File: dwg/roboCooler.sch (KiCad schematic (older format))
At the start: 37 parts, among them J1 CONN_02X25, J10 CONN_01X12, J11 CONN_01X12, J12 CONN_01X04, J13 CONN_01X04, J14 CONN_01X04, J15 CONN_01X04, J2 CONN_02X25, J3 CONN_01X04, J4 CONN_01X04, J5 CONN_01X02, J6 CONN_01X02, J7 CONN_01X02, J8 CONN_01X02, J9 CONN_01X06, P11 CONN_01X12, P12 CONN_01X04, P13 CONN_01X04, P14 CONN_01X04, P15 CONN_01X04, P3 CONN_01X04, P4 CONN_01X04, P5 CONN_01X02, P6 CONN_01X02, P7 CONN_01X02, P8 CONN_01X02, Q1 NMOS, Q2 NMOS, SW1 SW_PUSH, SW2 SW_PUSH, U1 MPR121, U2 4069, U3 HALL_EFFECT, U4 HALL_EFFECT

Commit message: Added pushbuttons to layout
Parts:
- removed P11: CONN_01X12, symbol CONN_01X12
- removed P12, P14: CONN_01X04, symbol CONN_01X04
- removed SW1, SW2: SW_PUSH, symbol SW_PUSH
- removed U1: MPR121, symbol MPR121
- added R12, R13: 10k, Resistors_SMD:R_0805_HandSoldering, symbol R
- added SW1, SW2: SPST_4PIN, roboCooler:D6C90, symbol SPST_4PIN
- D1, D2: footprint (none) -> Diodes_ThroughHole:Diode_P600_Vertical_AnodeUp
- J1, J2: footprint (none) -> Socket_Strips:Socket_Strip_Straight_2x25
- J10: footprint (none) -> Socket_Strips:Socket_Strip_Straight_1x12
- J11: footprint (none) -> Socket_Strips:Socket_Strip_Angled_1x12
- J3: footprint (none) -> Socket_Strips:Socket_Strip_Angled_1x04
- J5, J7: footprint (none) -> Socket_Strips:Socket_Strip_Angled_1x02
- Q1, Q2: footprint (none) -> Transistors_OldSowjetAera:OldSowjetaera_Transistor_Type-II_BigPads
- R1: footprint (none) -> Resistors_SMD:R_0805_HandSoldering
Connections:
- net labels added: PUSH_DB, PUSH_DN, PUSH_UP
- net labels removed: PUSH_1, PUSH_2
- wire segments 23 -> 29
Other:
- moved on the sheet: J9

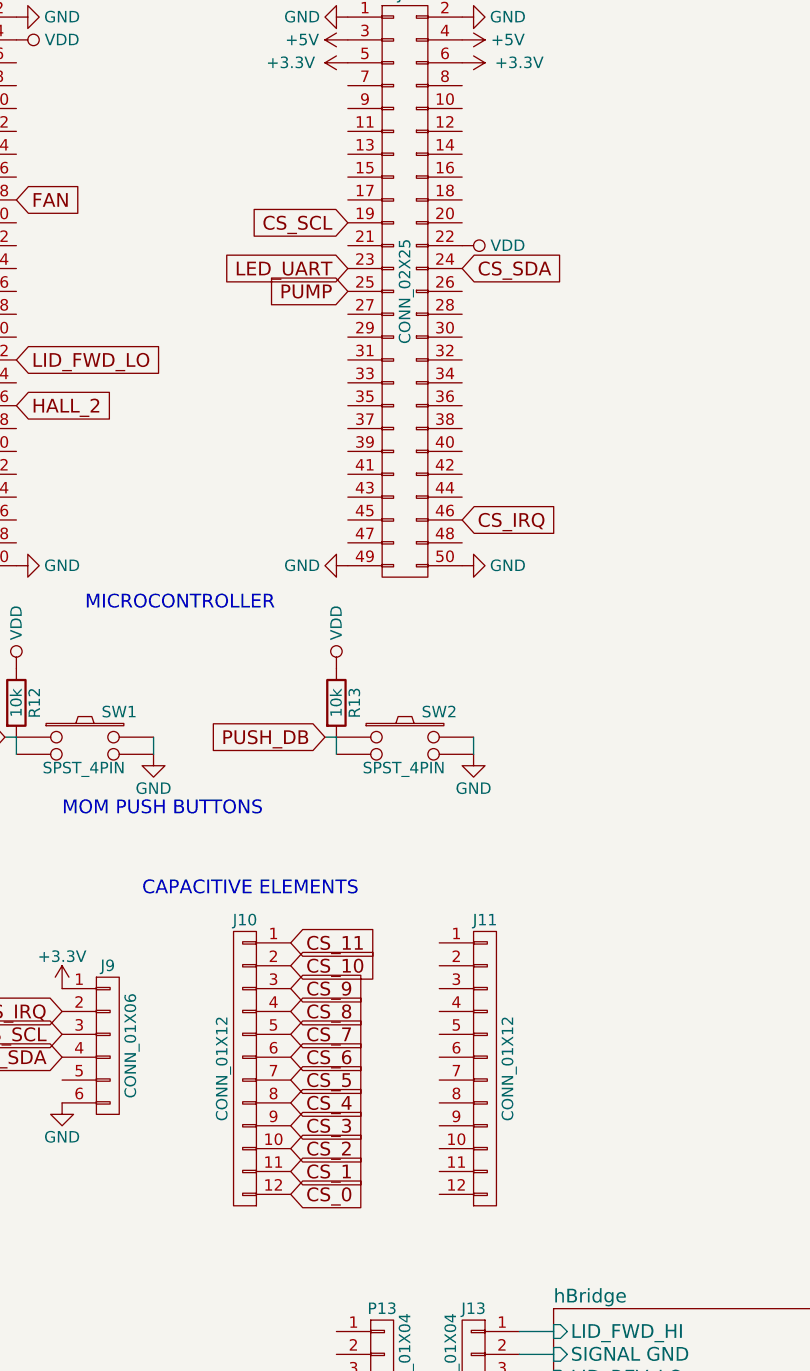
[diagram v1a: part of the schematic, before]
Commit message: added cap sense to layout
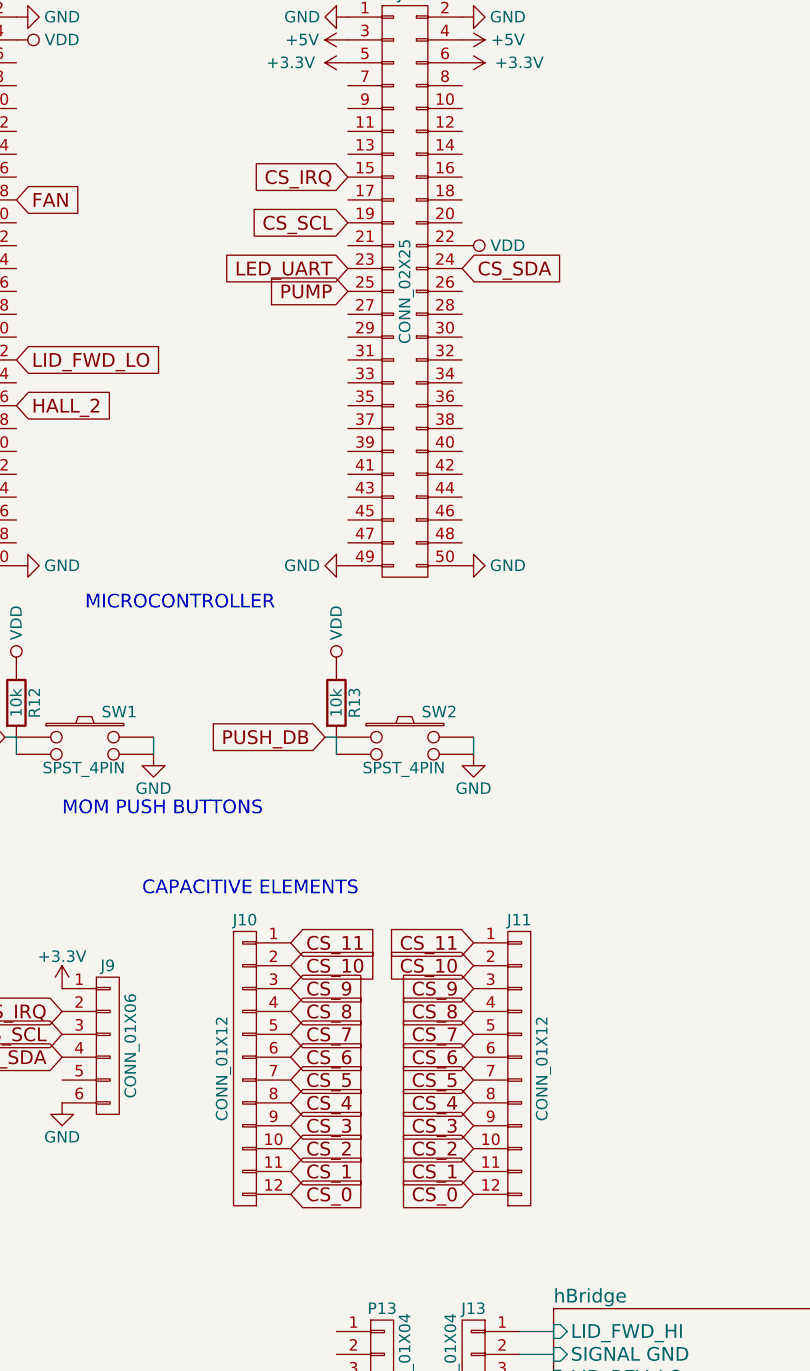
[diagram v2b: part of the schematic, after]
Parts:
- J9: footprint (none) -> Pin_Headers:Pin_Header_Straight_1x06
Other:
- moved on the sheet: J11
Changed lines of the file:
@@
 LIBS:valves
 LIBS:roboCooler
+LIBS:roboCooler-cache
 EELAYER 25 0
 EELAYER END
@@
 F 0 "J9" H 2100 5650 50  0000 C CNN
 F 1 "CONN_01X06" V 2200 5300 50  0000 C CNN
-F 2 "" H 2100 5300 60  0001 C CNN
+F 2 "Pin_Headers:Pin_Header_Straight_1x06" H 2100 5300 60  0001 C CNN
 F 3 "" H 2100 5300 60  0000 C CNN
 	1    2100 5300
@@
 Text GLabel 1900 5150 0    60   Input ~ 0
 CS_IRQ
-Text GLabel 3650 3000 2    60   Input ~ 0
+Text GLabel 3150 1500 0    60   Input ~ 0
 CS_IRQ
 $Comp
@@
 L CONN_01X12 J11
 U 1 1 569F9129
-P 3750 5400
-F 0 "J11" H 3750 6050 50  0000 C CNN
-F 1 "CONN_01X12" V 3850 5400 50  0000 C CNN
-F 2 "Socket_Strips:Socket_Strip_Angled_1x12" H 3750 5400 60  0001 C CNN
-F 3 "" H 3750 5400 60  0000 C CNN
-	1    3750 5400
+P 3900 5400
+F 0 "J11" H 3900 6050 50  0000 C CNN
+F 1 "CONN_01X12" V 4000 5400 50  0000 C CNN
+F 2 "Socket_Strips:Socket_Strip_Angled_1x12" H 3900 5400 60  0001 C CNN
+F 3 "" H 3900 5400 60  0000 C CNN
+	1    3900 5400
 	1    0    0    -1
 $EndComp
@@
 Wire Wire Line
 	1700 3950 1700 4025
+Text GLabel 3700 4850 0    60   Input ~ 0
+CS_11
+Text GLabel 3700 4950 0    60   Input ~ 0
+CS_10
+Text GLabel 3700 5050 0    60   Input ~ 0
+CS_9
+Text GLabel 3700 5150 0    60   Input ~ 0
+CS_8
+Text GLabel 3700 5250 0    60   Input ~ 0
+CS_7
+Text GLabel 3700 5350 0    60   Input ~ 0
+CS_6
+Text GLabel 3700 5450 0    60   Input ~ 0
+CS_5
+Text GLabel 3700 5550 0    60   Input ~ 0
+CS_4
+Text GLabel 3700 5650 0    60   Input ~ 0
+CS_3
+Text GLabel 3700 5750 0    60   Input ~ 0
+CS_2
+Text GLabel 3700 5850 0    60   Input ~ 0
+CS_1
+Text GLabel 3700 5950 0    60   Input ~ 0
+CS_0
 $EndSCHEMATC

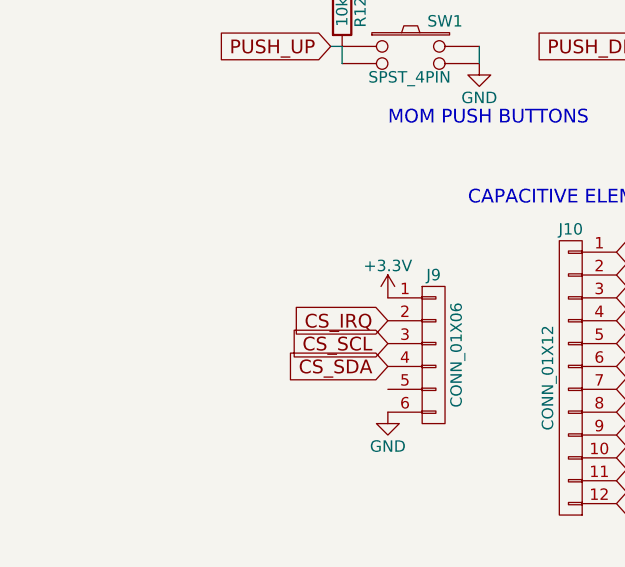
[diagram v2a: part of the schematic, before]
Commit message: added pull up resistors to cap sense i2c lines
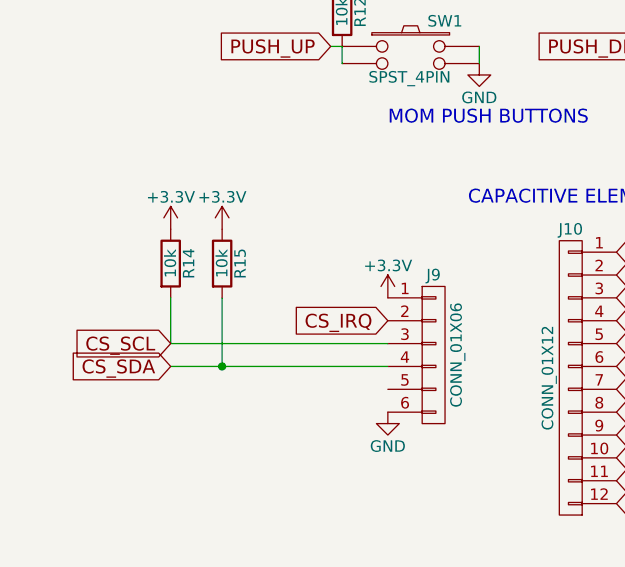
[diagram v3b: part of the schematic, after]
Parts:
- added R14, R15: 10k, Resistors_SMD:R_0805_HandSoldering, symbol R
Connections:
- wire segments 29 -> 33
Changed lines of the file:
@@
 Text GLabel 7500 2650 0    60   Input ~ 0
 FAN
-Text GLabel 1900 5350 0    60   Input ~ 0
+Text GLabel 950  5350 0    60   Input ~ 0
 CS_SDA
-Text GLabel 1900 5250 0    60   Input ~ 0
+Text GLabel 950  5250 0    60   Input ~ 0
 CS_SCL
 $Comp
@@
 	1    0    0    -1
 $EndComp
-Wire Wire Line
-	7800 3550 7800 3650
-Wire Wire Line
-	7700 3400 7800 3400
-Wire Wire Line
-	7800 3600 7700 3600
-Connection ~ 7800 3600
-Wire Wire Line
-	7800 2350 7800 2450
-Wire Wire Line
-	7650 2200 7800 2200
-Wire Wire Line
-	7800 2400 7650 2400
-Connection ~ 7800 2400
-Wire Wire Line
-	7350 1400 7800 1400
-Wire Wire Line
-	7300 5350 9800 5350
-Wire Wire Line
-	7300 4700 9800 4700
-Wire Wire Line
-	7800 2200 7800 2250
-Wire Wire Line
-	7800 3400 7800 3450
-Wire Notes Line
-	8600 1450 9750 1450
-Wire Notes Line
-	8600 2300 9750 2300
-Wire Notes Line
-	8600 3500 9750 3500
-Wire Wire Line
-	7750 4600 9800 4600
-Wire Wire Line
-	7750 4800 9800 4800
-Wire Wire Line
-	7750 5250 9800 5250
-Wire Wire Line
-	7750 5450 9800 5450
-Wire Wire Line
-	3900 6550 4050 6550
-Wire Wire Line
-	3900 6650 4050 6650
-Wire Wire Line
-	3900 6750 4050 6750
-Wire Wire Line
-	4050 6850 3900 6850
-Wire Wire Line
-	3900 7150 4050 7150
-Wire Wire Line
-	4050 7250 3900 7250
-Wire Wire Line
-	3900 7350 4050 7350
-Wire Wire Line
-	4050 7450 3900 7450
-Wire Wire Line
-	2300 3950 2300 4025
 $Comp
 L GND #PWR037
@@
 	1    0    0    -1
 $EndComp
-Wire Wire Line
-	3050 3950 3100 3950
-Wire Wire Line
-	3100 3950 3100 4025
-Wire Wire Line
-	3700 3950 3700 4025
 $Comp
 L VDD #PWR038
@@
 	1    0    0    -1
 $EndComp
-Wire Wire Line
-	1650 3950 1700 3950
-Wire Wire Line
-	1700 3950 1700 4025
 Text GLabel 3700 4850 0    60   Input ~ 0
 CS_11
@@
 Text GLabel 3700 5950 0    60   Input ~ 0
 CS_0
+$Comp
+L R R14
+U 1 1 5766F109
+P 950 4900
+F 0 "R14" V 1030 4900 50  0000 C CNN
+F 1 "10k" V 950 4900 50  0000 C CNN
+F 2 "Resistors_SMD:R_0805_HandSoldering" V 880 4900 30  0001 C CNN
+F 3 "" H 950 4900 30  0000 C CNN
+	1    950  4900
+	1    0    0    -1
+$EndComp
+$Comp
+L R R15
+U 1 1 5766F2F6
+P 1175 4900
+F 0 "R15" V 1255 4900 50  0000 C CNN
+F 1 "10k" V 1175 4900 50  0000 C CNN
+F 2 "Resistors_SMD:R_0805_HandSoldering" V 1105 4900 30  0001 C CNN
+F 3 "" H 1175 4900 30  0000 C CNN
+	1    1175 4900
+	1    0    0    -1
+$EndComp
+$Comp
+L +3.3V #PWR040
+U 1 1 5766F440
+P 1175 4750
+F 0 "#PWR040" H 1175 4600 50  0001 C CNN
+F 1 "+3.3V" H 1175 4890 50  0000 C CNN
+F 2 "" H 1175 4750 60  0000 C CNN
+F 3 "" H 1175 4750 60  0000 C CNN
+	1    1175 4750
+	1    0    0    -1
+$EndComp
+$Comp
+L +3.3V #PWR041
+U 1 1 5766F4F6
+P 950 4750
+F 0 "#PWR041" H 950 4600 50  0001 C CNN
+F 1 "+3.3V" H 950 4890 50  0000 C CNN
+F 2 "" H 950 4750 60  0000 C CNN
+F 3 "" H 950 4750 60  0000 C CNN
+	1    950  4750
+	1    0    0    -1
+$EndComp
+Wire Wire Line
+	7800 3550 7800 3650
+Wire Wire Line
+	7700 3400 7800 3400
+Wire Wire Line
+	7800 3600 7700 3600
+Connection ~ 7800 3600
+Wire Wire Line
+	7800 2350 7800 2450
+Wire Wire Line
+	7650 2200 7800 2200
+Wire Wire Line
+	7800 2400 7650 2400
+Connection ~ 7800 2400
+Wire Wire Line
+	7350 1400 7800 1400
+Wire Wire Line
+	7300 5350 9800 5350
+Wire Wire Line
+	7300 4700 9800 4700
+Wire Wire Line
+	7800 2200 7800 2250
+Wire Wire Line
+	7800 3400 7800 3450
+Wire Notes Line
+	8600 1450 9750 1450
+Wire Notes Line
+	8600 2300 9750 2300
+Wire Notes Line
+	8600 3500 9750 3500
+Wire Wire Line
+	7750 4600 9800 4600
+Wire Wire Line
+	7750 4800 9800 4800
+Wire Wire Line
+	7750 5250 9800 5250
+Wire Wire Line
+	7750 5450 9800 5450
+Wire Wire Line
+	3900 6550 4050 6550
+Wire Wire Line
+	3900 6650 4050 6650
+Wire Wire Line
+	3900 6750 4050 6750
+Wire Wire Line
+	4050 6850 3900 6850
+Wire Wire Line
+	3900 7150 4050 7150
+Wire Wire Line
+	4050 7250 3900 7250
+Wire Wire Line
+	3900 7350 4050 7350
+Wire Wire Line
+	4050 7450 3900 7450
+Wire Wire Line
+	2300 3950 2300 4025
+Wire Wire Line
+	3050 3950 3100 3950
+Wire Wire Line
+	3100 3950 3100 4025
+Wire Wire Line
+	3700 3950 3700 4025
+Wire Wire Line
+	1650 3950 1700 3950
+Wire Wire Line
+	1700 3950 1700 4025
+Wire Wire Line
+	950  5050 950  5250
+Wire Wire Line
+	950  5250 1900 5250
+Wire Wire Line
+	950  5350 1900 5350
+Wire Wire Line
+	1175 5050 1175 5350
+Connection ~ 1175 5350
 $EndSCHEMATC

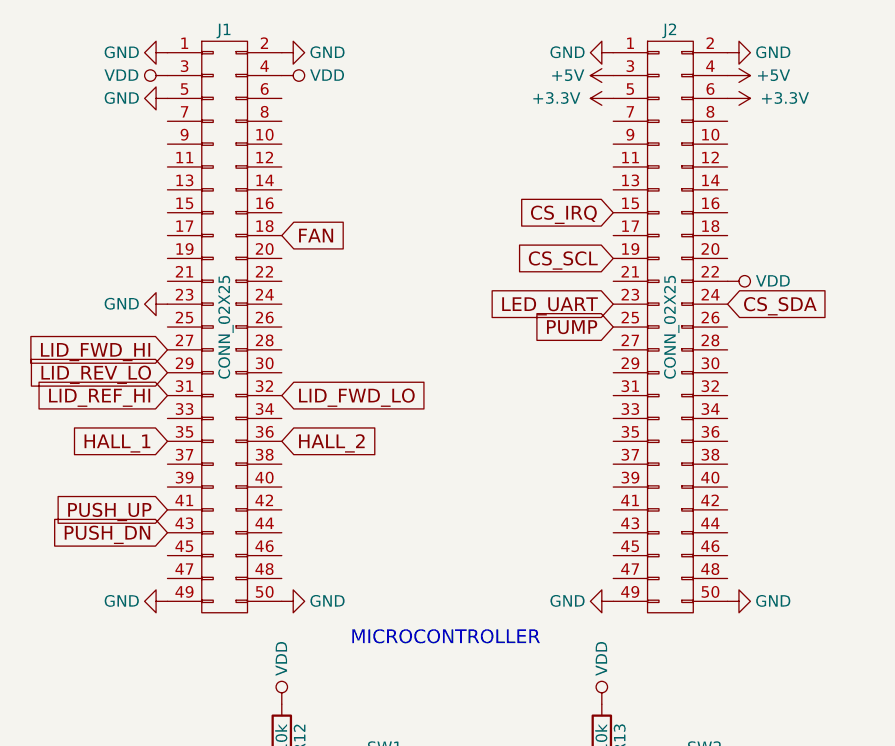
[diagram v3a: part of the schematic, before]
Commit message: added no connects to mcu connectors
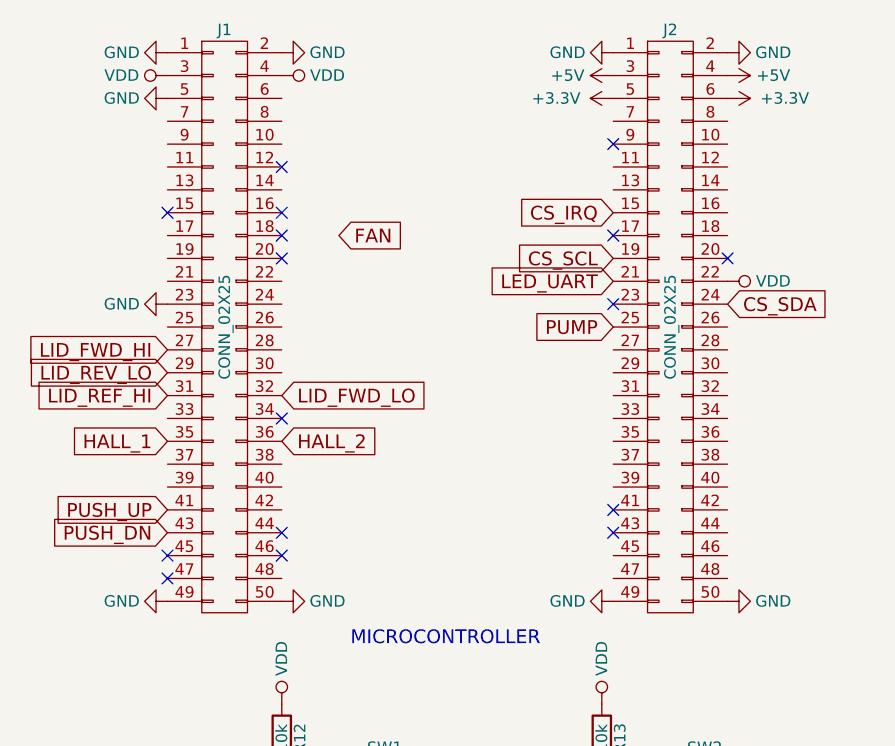
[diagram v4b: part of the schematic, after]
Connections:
- no-connect marks 0 -> 16
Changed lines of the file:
@@
 	1    0    0    -1
 $EndComp
-Text GLabel 3150 1900 0    60   Input ~ 0
+Text GLabel 3150 1800 0    60   Input ~ 0
 LED_UART
 Text GLabel 6450 1400 0    60   Input ~ 0
@@
 Text GLabel 7500 3850 0    60   Input ~ 0
 PUMP
-Text GLabel 1700 1600 2    60   Input ~ 0
+Text GLabel 1950 1600 2    60   Input ~ 0
 FAN
 Text GLabel 7500 2650 0    60   Input ~ 0
@@
 	1175 5050 1175 5350
 Connection ~ 1175 5350
+NoConn ~ 1700 1300
+NoConn ~ 1700 1500
+NoConn ~ 1700 1600
+NoConn ~ 1700 1700
+NoConn ~ 1700 2400
+NoConn ~ 1700 2900
+NoConn ~ 1700 3000
+NoConn ~ 1200 3000
+NoConn ~ 1200 3100
+NoConn ~ 1200 1500
+NoConn ~ 3150 1900
+NoConn ~ 3150 2800
+NoConn ~ 3150 2900
+NoConn ~ 3650 1700
+NoConn ~ 3150 1600
+NoConn ~ 3150 1200
 $EndSCHEMATC
